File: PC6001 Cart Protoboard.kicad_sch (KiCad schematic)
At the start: 20 parts, among them J1 PC-6001 edge connector, SW1 PicoReset, SW2 EspReset, SW3 Button A, U2 ESP32-DevKitC, U3 74LS32, U4 microSD-Breakout, U5 74LS08, U6 SN74LVC245AN, U7 SN74LVC245AN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

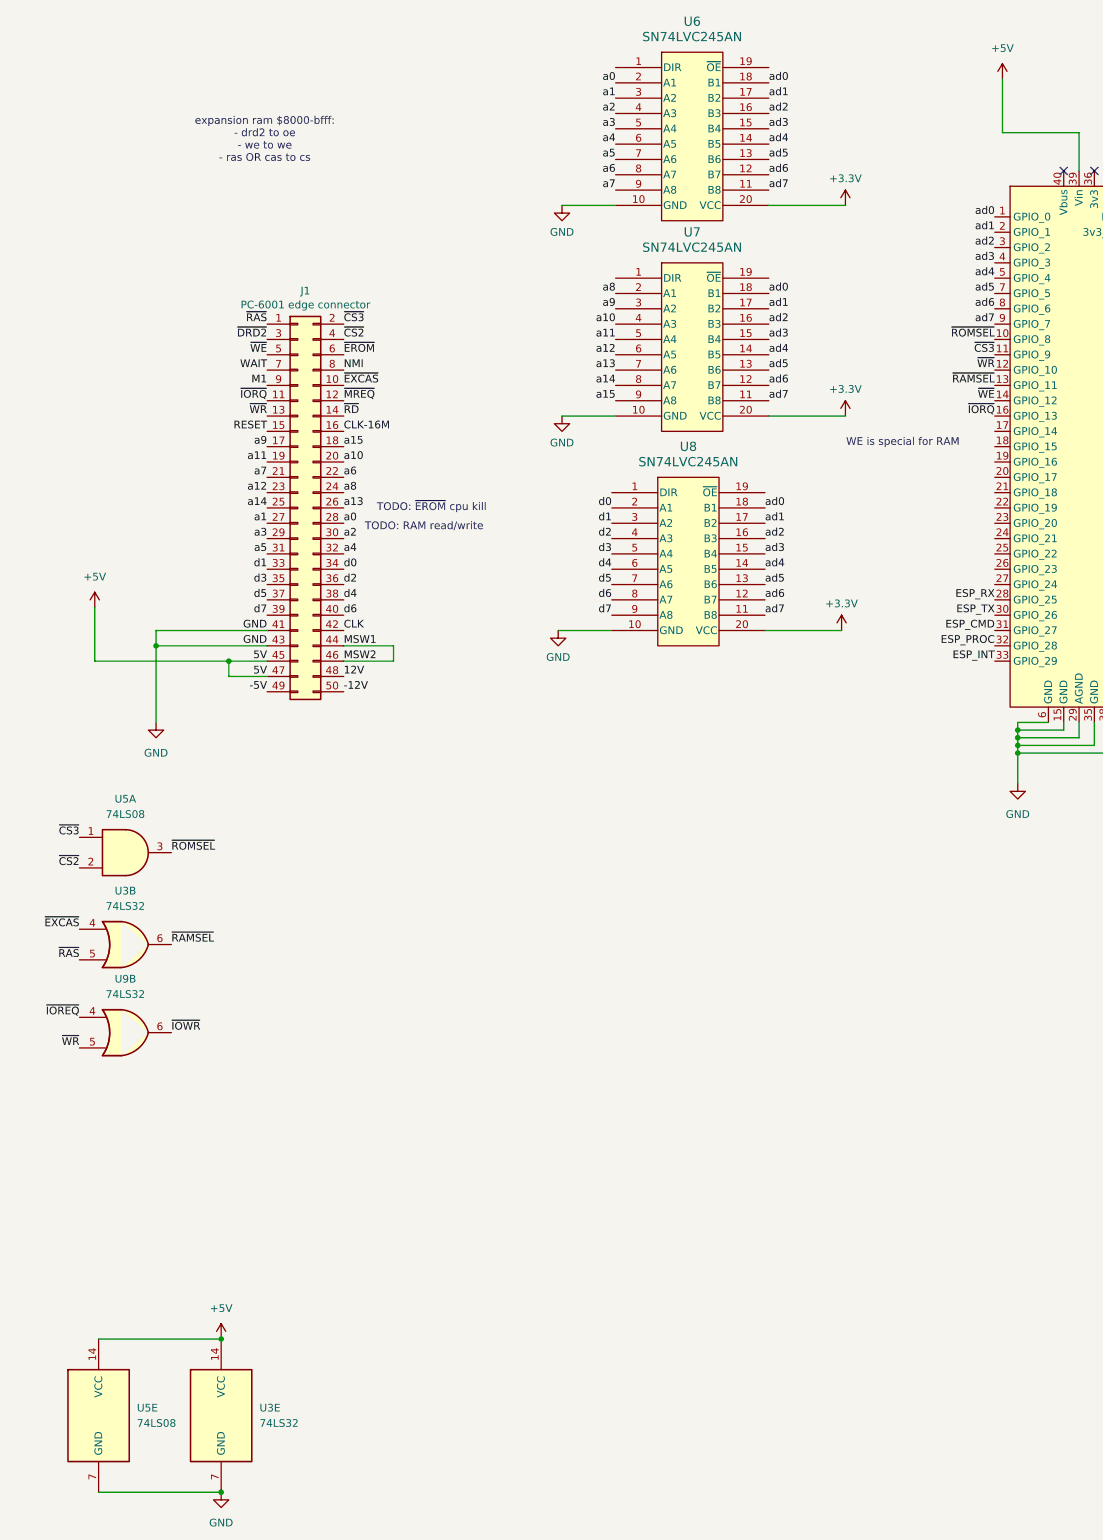
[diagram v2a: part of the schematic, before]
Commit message: Buffer control pins
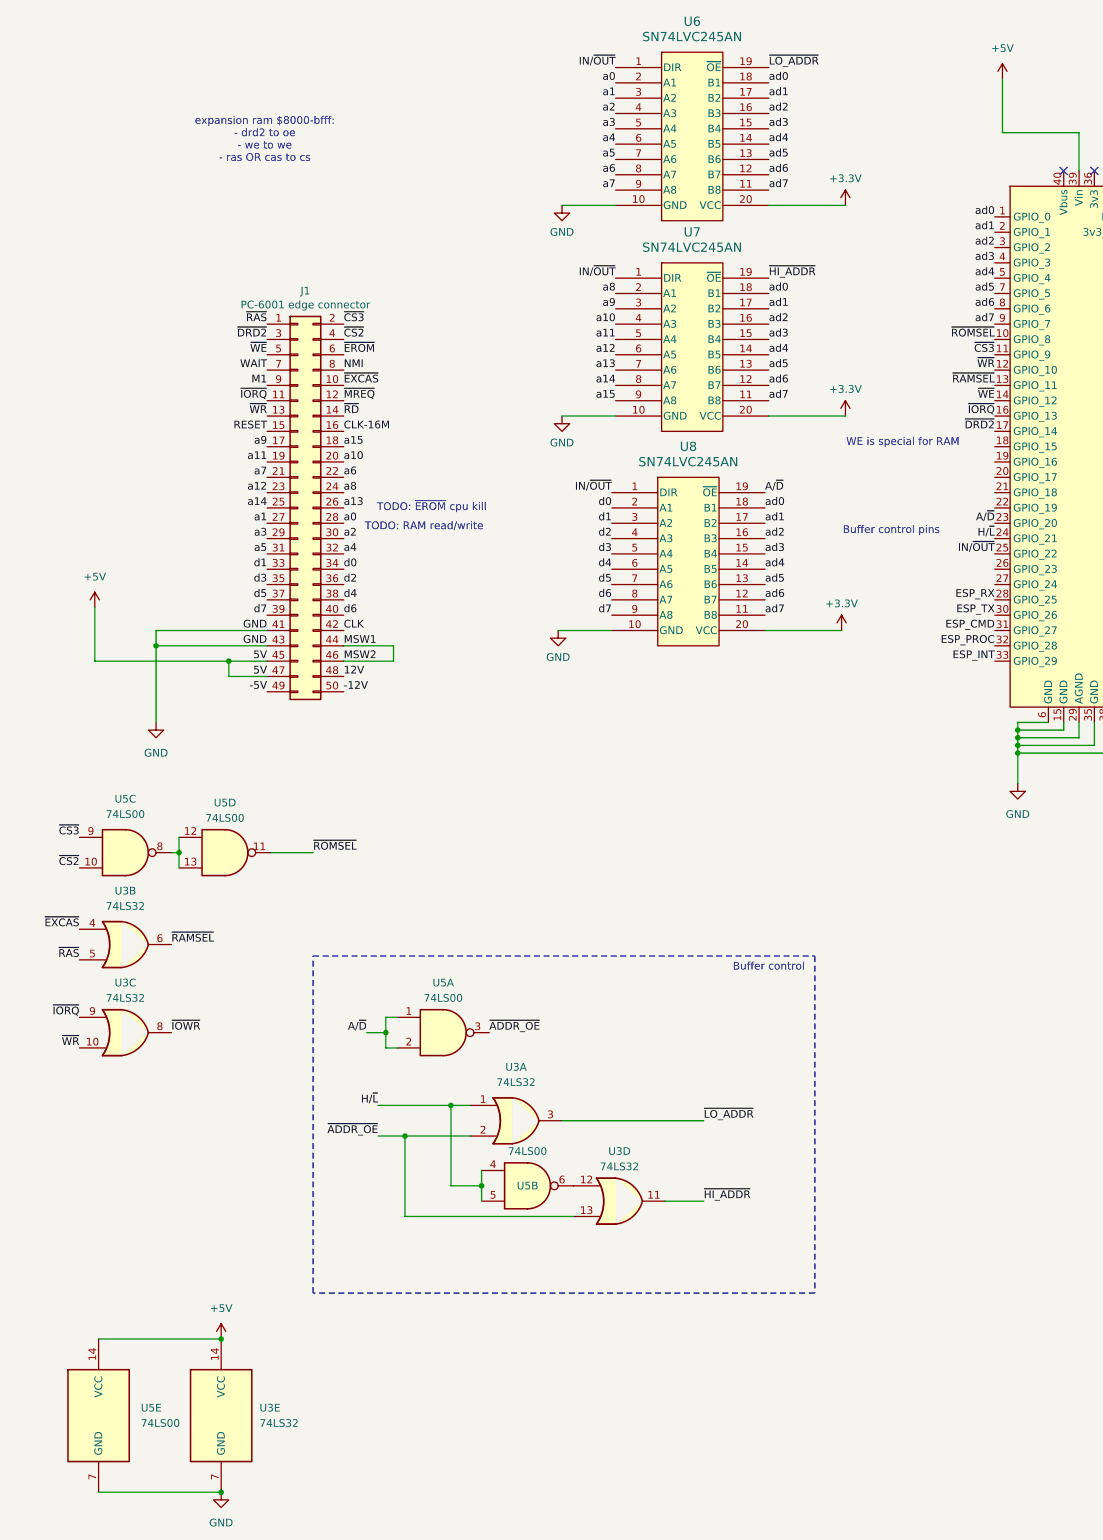
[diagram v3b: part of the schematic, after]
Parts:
- removed U5: 74LS08, Package_DIP:DIP-14_W7.62mm_Socket_LongPads, symbol 74xx:74LS08
- removed U9: 74LS32, Package_DIP:DIP-14_W7.62mm_Socket_LongPads, symbol 74xx:74LS32
- added unit 1 of U3
- added unit 4 of U3
- added unit 3 of U3
- added U5: 74LS00, symbol 74xx:74LS00
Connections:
- net +5V: now also U5.14 (VCC)
- net GND: now also U5.7 (GND)
- net ~{CS2}: now also U5.10
- net ~{CS3}: now also U5.9
- net ~{DRD2}: now also U1.17 (GPIO_14)
- net ~{IORQ}: now also U3.9
- net ~{IOWR}: now also U3.8
- net ~{ROMSEL}: now also U5.11
- net ~{WR}: now also U3.10
- net A/~{D}: now reaches U1.23 (GPIO_20)
- net A/~{D}: now also U8.19 (~{OE}), U5.1, U5.2
- net H/~{L}: now reaches U1.24 (GPIO_21)
- net H/~{L}: now also U3.1, U5.4, U5.5
- net IN/~{OUT}: now reaches U1.25 (GPIO_22)
- net IN/~{OUT}: now also U6.1 (DIR), U7.1 (DIR), U8.1 (DIR)
- net ~{LO_ADDR}: now reaches U6.19 (~{OE})
- net ~{LO_ADDR}: now also U3.3
- net ~{HI_ADDR}: now reaches U7.19 (~{OE})
- net ~{HI_ADDR}: now also U3.11
- new net: U3.12, U5.6
- new net: U5.12, U5.13, U5.8
- new net ~{ADDR_OE}: U3.13, U3.2, U5.3
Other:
- note added: "Buffer control"
- note added: "Buffer control pins"

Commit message: Place nand gate
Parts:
- U5: footprint (none) -> Package_DIP:DIP-14_W7.62mm_Socket_LongPads
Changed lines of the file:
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@@
 			)
 		)
-		(property "Footprint" ""
+		(property "Footprint" "Package_DIP:DIP-14_W7.62mm_Socket_LongPads"
 			(at 27.94 166.37 0)
 			(effects
@@
 			)
 		)
-		(property "Footprint" ""
+		(property "Footprint" "Package_DIP:DIP-14_W7.62mm_Socket_LongPads"
 			(at 23.495 259.715 0)
 			(effects
@@
 			)
 		)
-		(property "Footprint" ""
+		(property "Footprint" "Package_DIP:DIP-14_W7.62mm_Socket_LongPads"
 			(at 94.615 221.615 0)
 			(effects
@@
 			)
 		)
-		(property "Footprint" ""
+		(property "Footprint" "Package_DIP:DIP-14_W7.62mm_Socket_LongPads"
 			(at 80.645 196.215 0)
 			(effects
@@
 			)
 		)
-		(property "Footprint" ""
+		(property "Footprint" "Package_DIP:DIP-14_W7.62mm_Socket_LongPads"
 			(at 44.45 166.37 0)
 			(effects

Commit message: Fully routed
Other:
- note added: "TODO: should 3.3v come from the RP?"
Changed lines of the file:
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@@
+		)
+	)
+	(text "TODO: should 3.3v come from the RP?"
+		(exclude_from_sim no)
+		(at 216.535 83.82 0)
+		(effects
+			(font
+				(size 1.27 1.27)
+			)
 		)
 	)

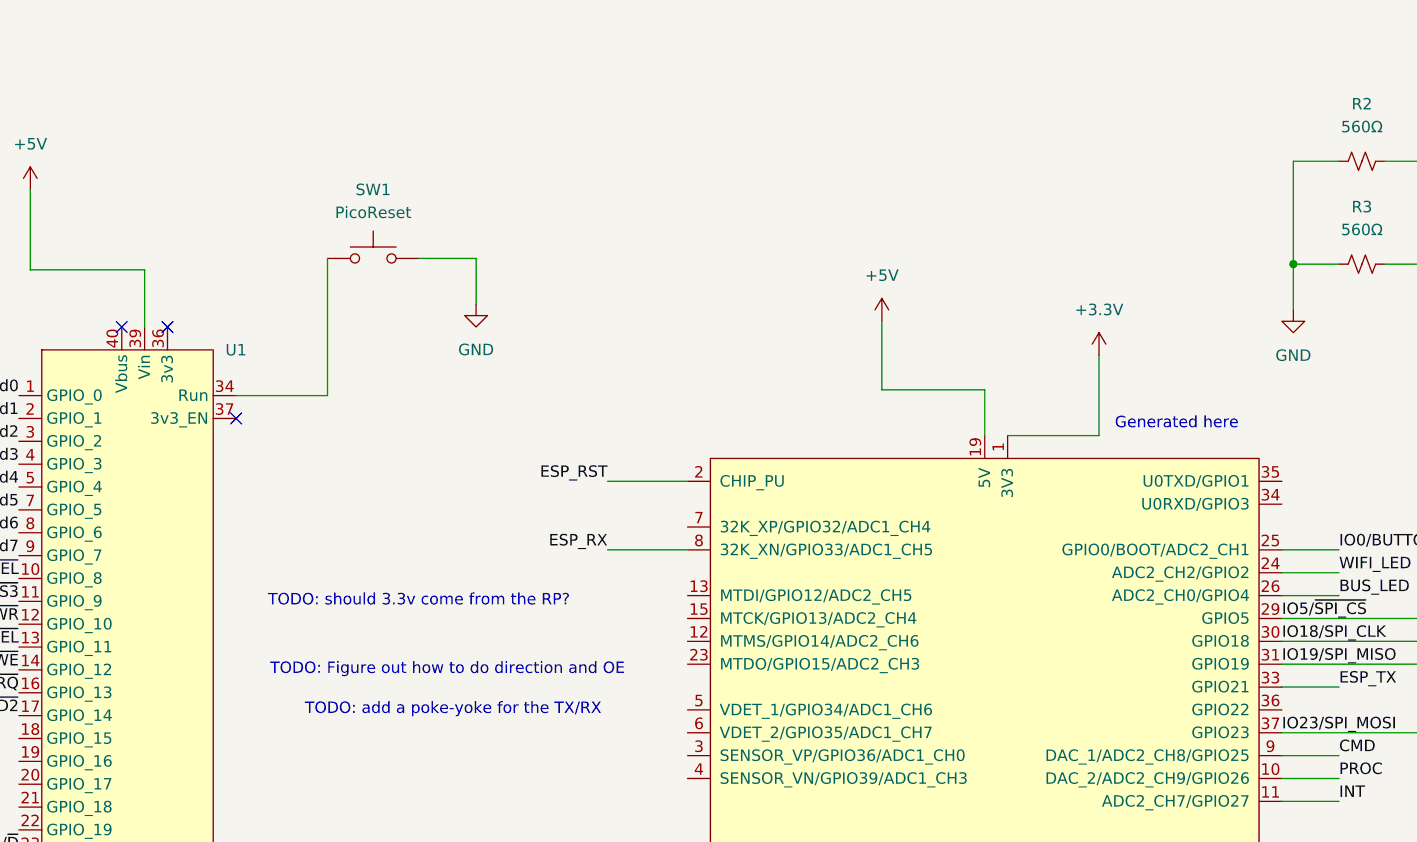
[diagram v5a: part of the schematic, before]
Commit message: Source 3v3 from Pico for now
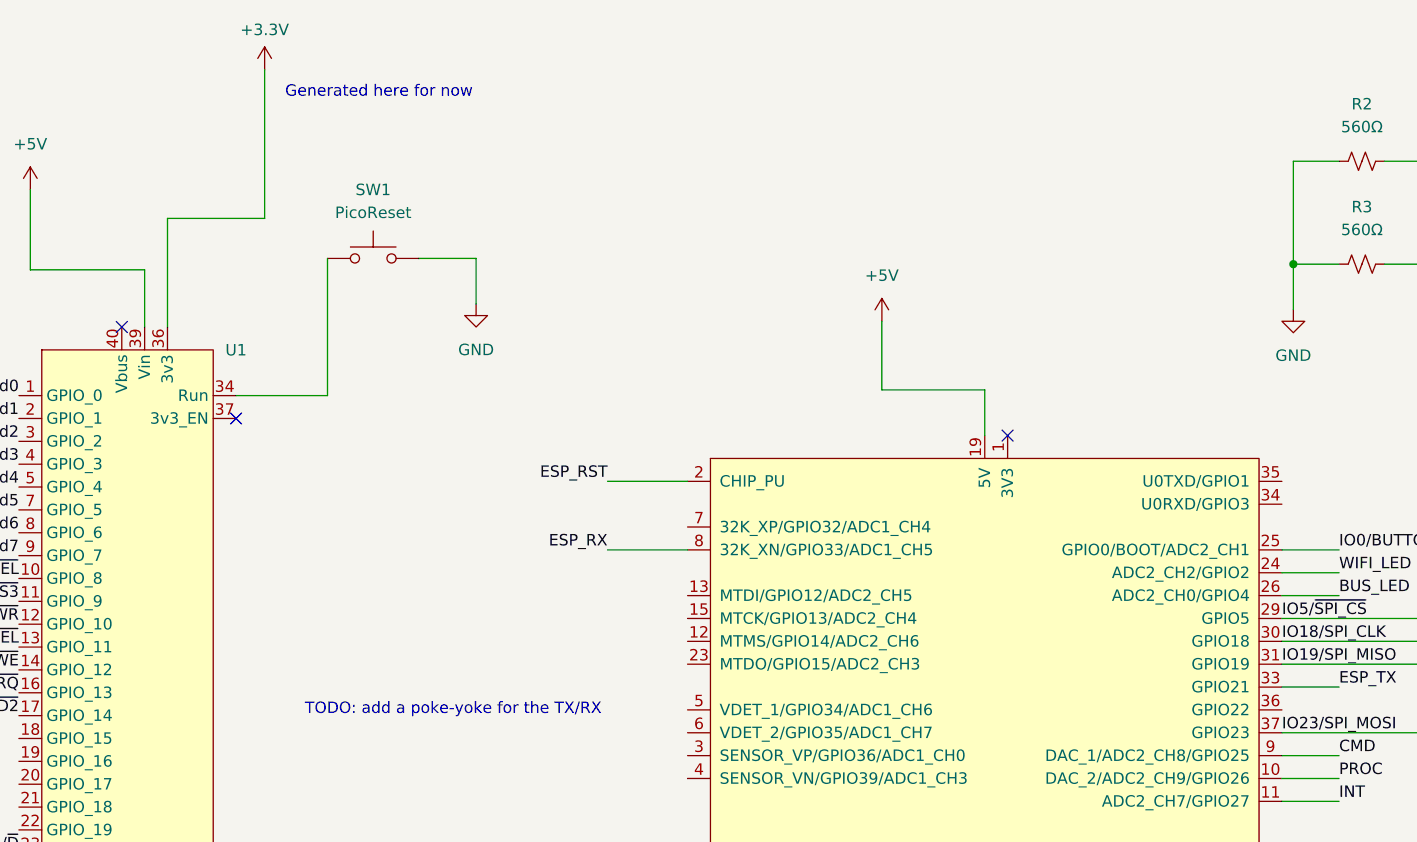
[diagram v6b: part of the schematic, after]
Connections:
- net +3.3V: now also U1.36 (3v3); no longer U2.1 (3V3)
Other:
- note added: "Generated here for now"
- note removed: "Generated here"
- note removed: "TODO: Figure out how to do direction and OE"
- note removed: "TODO: should 3.3v come from the RP?"
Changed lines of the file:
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@@
 	)
 	(no_connect
-		(at 188.595 53.34)
+		(at 281.94 65.405)
 	)
 	(no_connect
@@
 	(wire
 		(pts
-			(xy 100.33 93.98) (xy 109.22 93.98)
+			(xy 188.595 41.275) (xy 188.595 53.34)
 		)
 		(stroke
@@
 	(wire
 		(pts
-			(xy 67.945 196.215) (xy 71.12 196.215)
+			(xy 100.33 93.98) (xy 109.22 93.98)
 		)
 		(stroke
@@
 	(wire
 		(pts
-			(xy 307.34 186.69) (xy 312.42 186.69)
+			(xy 67.945 196.215) (xy 71.12 196.215)
 		)
 		(stroke
@@
 	(wire
 		(pts
-			(xy 307.34 176.53) (xy 313.69 176.53)
+			(xy 307.34 186.69) (xy 312.42 186.69)
 		)
 		(stroke
@@
 	(wire
 		(pts
-			(xy 340.36 123.825) (xy 356.87 123.825)
+			(xy 307.34 176.53) (xy 313.69 176.53)
 		)
 		(stroke
@@
 	(wire
 		(pts
-			(xy 191.135 149.86) (xy 175.895 149.86)
+			(xy 199.39 41.275) (xy 188.595 41.275)
 		)
 		(stroke
@@
 	(wire
 		(pts
-			(xy 100.33 210.82) (xy 123.825 210.82)
+			(xy 340.36 123.825) (xy 356.87 123.825)
 		)
 		(stroke
@@
 	(wire
 		(pts
-			(xy 33.02 132.08) (xy 33.02 129.54)
+			(xy 191.135 149.86) (xy 175.895 149.86)
 		)
 		(stroke
@@
 	(wire
 		(pts
-			(xy 33.02 132.08) (xy 51.435 132.08)
+			(xy 100.33 210.82) (xy 123.825 210.82)
 		)
 		(stroke
@@
 	(wire
 		(pts
-			(xy 292.1 56.515) (xy 292.1 65.405)
+			(xy 33.02 132.08) (xy 33.02 129.54)
 		)
 		(stroke
@@
 	(wire
 		(pts
-			(xy 359.41 103.505) (xy 359.41 106.045)
+			(xy 33.02 132.08) (xy 51.435 132.08)
 		)
 		(stroke
@@
 	(wire
 		(pts
-			(xy 292.1 65.405) (xy 281.94 65.405)
+			(xy 359.41 103.505) (xy 359.41 106.045)
 		)
 		(stroke
@@
 	(wire
 		(pts
+			(xy 199.39 24.765) (xy 199.39 41.275)
+		)
+		(stroke
+			(width 0)
+			(type default)
+		)
+	)
+	(wire
+		(pts
 			(xy 74.295 213.36) (xy 74.295 226.695)
 		)
@@
 		)
 	)
-	(text "TODO: Figure out how to do direction and OE"
-		(exclude_from_sim no)
-		(at 219.71 91.44 0)
-		(effects
-			(font
-				(size 1.27 1.27)
-			)
-		)
-	)
 	(text "WE is special for RAM"
 		(exclude_from_sim no)
@@
 		)
 	)
-	(text "Generated here"
-		(exclude_from_sim no)
-		(at 300.736 64.135 0)
-		(effects
-			(font
-				(size 1.27 1.27)
-			)
-		)
-	)
 	(text "TODO: RAM read/write"
 		(exclude_from_sim no)
@@
 		)
 	)
-	(text "TODO: should 3.3v come from the RP?"
+	(text "http://p6ers.net/mm/pc-6001/dev/flashromcard/16k.html for 16K"
 		(exclude_from_sim no)
-		(at 216.535 83.82 0)
+		(at 289.56 151.765 0)
 		(effects
 			(font
 				(size 1.27 1.27)
 			)
+			(justify left bottom)
 		)
 	)
-	(text "http://p6ers.net/mm/pc-6001/dev/flashromcard/16k.html for 16K"
+	(text "expansion ram $8000-bfff:\n- drd2 to oe\n- we to we\n- ras OR cas to cs"
 		(exclude_from_sim no)
-		(at 289.56 151.765 0)
+		(at 51.054 48.26 0)
 		(effects
 			(font
 				(size 1.27 1.27)
 			)
-			(justify left bottom)
 		)
 	)
-	(text "expansion ram $8000-bfff:\n- drd2 to oe\n- we to we\n- ras OR cas to cs"
+	(text "Generated here for now"
 		(exclude_from_sim no)
-		(at 51.054 48.26 0)
+		(at 212.09 27.305 0)
 		(effects
 			(font
@@
 	)
 	(symbol
-		(lib_id "power:+3.3V")
-		(at 292.1 56.515 0)
-		(unit 1)
-		(exclude_from_sim no)
-		(in_bom yes)
-		(on_board yes)
-		(dnp no)
-		(fields_autoplaced yes)
-		(property "Reference" "#PWR08"
-			(at 292.1 60.325 0)
-			(effects
-				(font
-					(size 1.27 1.27)
-				)
-				(hide yes)
-			)
-		)
-		(property "Value" "+3.3V"
-			(at 292.1 51.435 0)
-			(effects
-				(font
-					(size 1.27 1.27)
-				)
-			)
-		)
-		(property "Footprint" ""
-			(at 292.1 56.515 0)
-			(effects
-				(font
-					(size 1.27 1.27)
-				)
-				(hide yes)
-			)
-		)
-		(property "Datasheet" ""
-			(at 292.1 56.515 0)
-			(effects
-				(font
-					(size 1.27 1.27)
-				)
-				(hide yes)
-			)
-		)
-		(property "Description" "Power symbol creates a global label with name \"+3.3V\""
-			(at 292.1 56.515 0)
-			(effects
-				(font
-					(size 1.27 1.27)
-				)
-				(hide yes)
-			)
-		)
-		(pin "1"
-		)
-		(instances
-			(project ""
-				(path "/43e41326-819e-40e7-9c3a-9c7b5d01c509"
-					(reference "#PWR08")
-					(unit 1)
-				)
-			)
-		)
-	)
-	(symbol
 		(lib_id "74lvc245an:SN74LVC245AN")
 		(at 93.98 36.195 0)
@@
 					(unit 1)
 				)
+			)
+		)
+	)
+	(symbol
+		(lib_id "power:+3.3V")
+		(at 199.39 24.765 0)
+		(unit 1)
+		(exclude_from_sim no)
+		(in_bom yes)
+		(on_board yes)
+		(dnp no)
+		(fields_autoplaced yes)
+		(property "Reference" "#PWR08"
+			(at 199.39 28.575 0)
+			(effects
+				(font
+					(size 1.27 1.27)
+				)
+				(hide yes)
+			)
+		)
+		(property "Value" "+3.3V"
+			(at 199.39 20.32 0)
+			(effects
+				(font
+					(size 1.27 1.27)
+				)
+			)
+		)
+		(property "Footprint" ""
+			(at 199.39 24.765 0)
+			(effects
+				(font
+					(size 1.27 1.27)
+				)
+				(hide yes)
+			)
+		)
+		(property "Datasheet" ""
+			(at 199.39 24.765 0)
+			(effects
+				(font
+					(size 1.27 1.27)
+				)
+				(hide yes)
+			)
+		)
+		(property "Description" "Power symbol creates a global label with name \"+3.3V\""
+			(at 199.39 24.765 0)
+			(effects
+				(font
+					(size 1.27 1.27)
+				)
+				(hide yes)
+			)
+		)
+		(pin "1"
+		)
+		(instances
+			(project ""
+				(path "/43e41326-819e-40e7-9c3a-9c7b5d01c509"
+					(reference "#PWR08")
+					(unit 1)
+				)

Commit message: ESP_INT restored
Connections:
- net INT is gone; now on net ESP_INT: U2.11 (ADC2_CH7/GPIO27)
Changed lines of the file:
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@@
 		)
 	)
-	(label "INT"
+	(label "ESP_INT"
 		(at 318.77 106.045 0)
 		(fields_autoplaced yes)

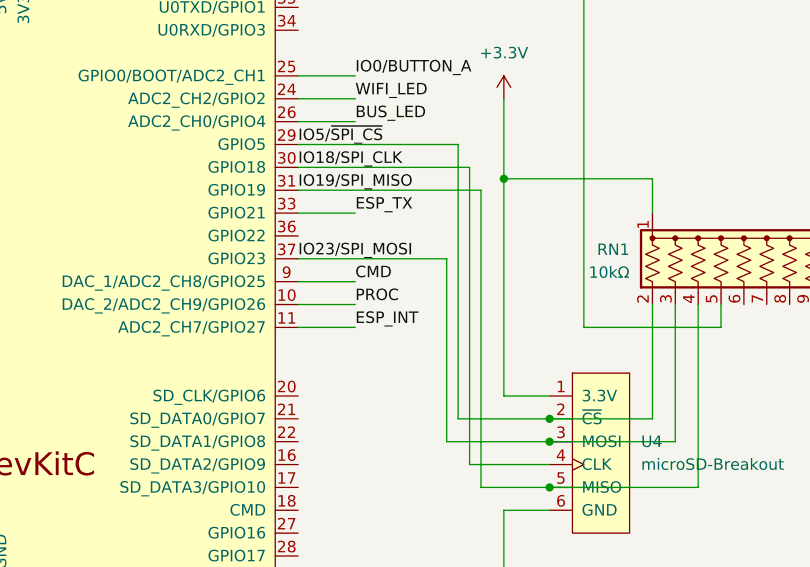
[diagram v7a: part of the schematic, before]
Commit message: Restore ESP_CMD, ESP_PROC
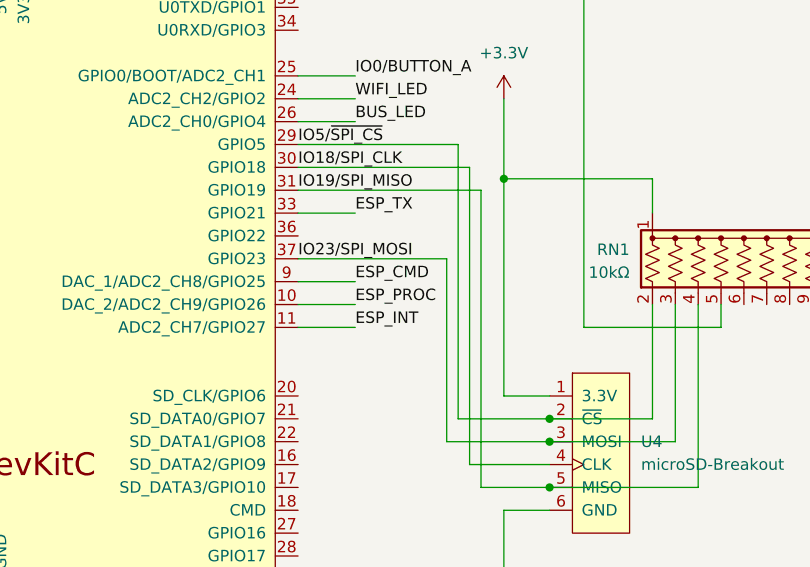
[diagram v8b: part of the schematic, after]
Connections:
- net CMD is gone; now on net ESP_CMD: U2.9 (DAC_1/ADC2_CH8/GPIO25)
- net PROC is gone; now on net ESP_PROC: U2.10 (DAC_2/ADC2_CH9/GPIO26)
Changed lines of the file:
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@@
 		)
 	)
-	(label "CMD"
+	(label "ESP_CMD"
 		(at 318.77 100.965 0)
 		(fields_autoplaced yes)
@@
 		)
 	)
-	(label "PROC"
+	(label "ESP_PROC"
 		(at 318.77 103.505 0)
 		(fields_autoplaced yes)
